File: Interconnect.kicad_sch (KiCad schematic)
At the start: 2 parts, among them J8 Interconnect-CPU, J9 Interconnect-PCH

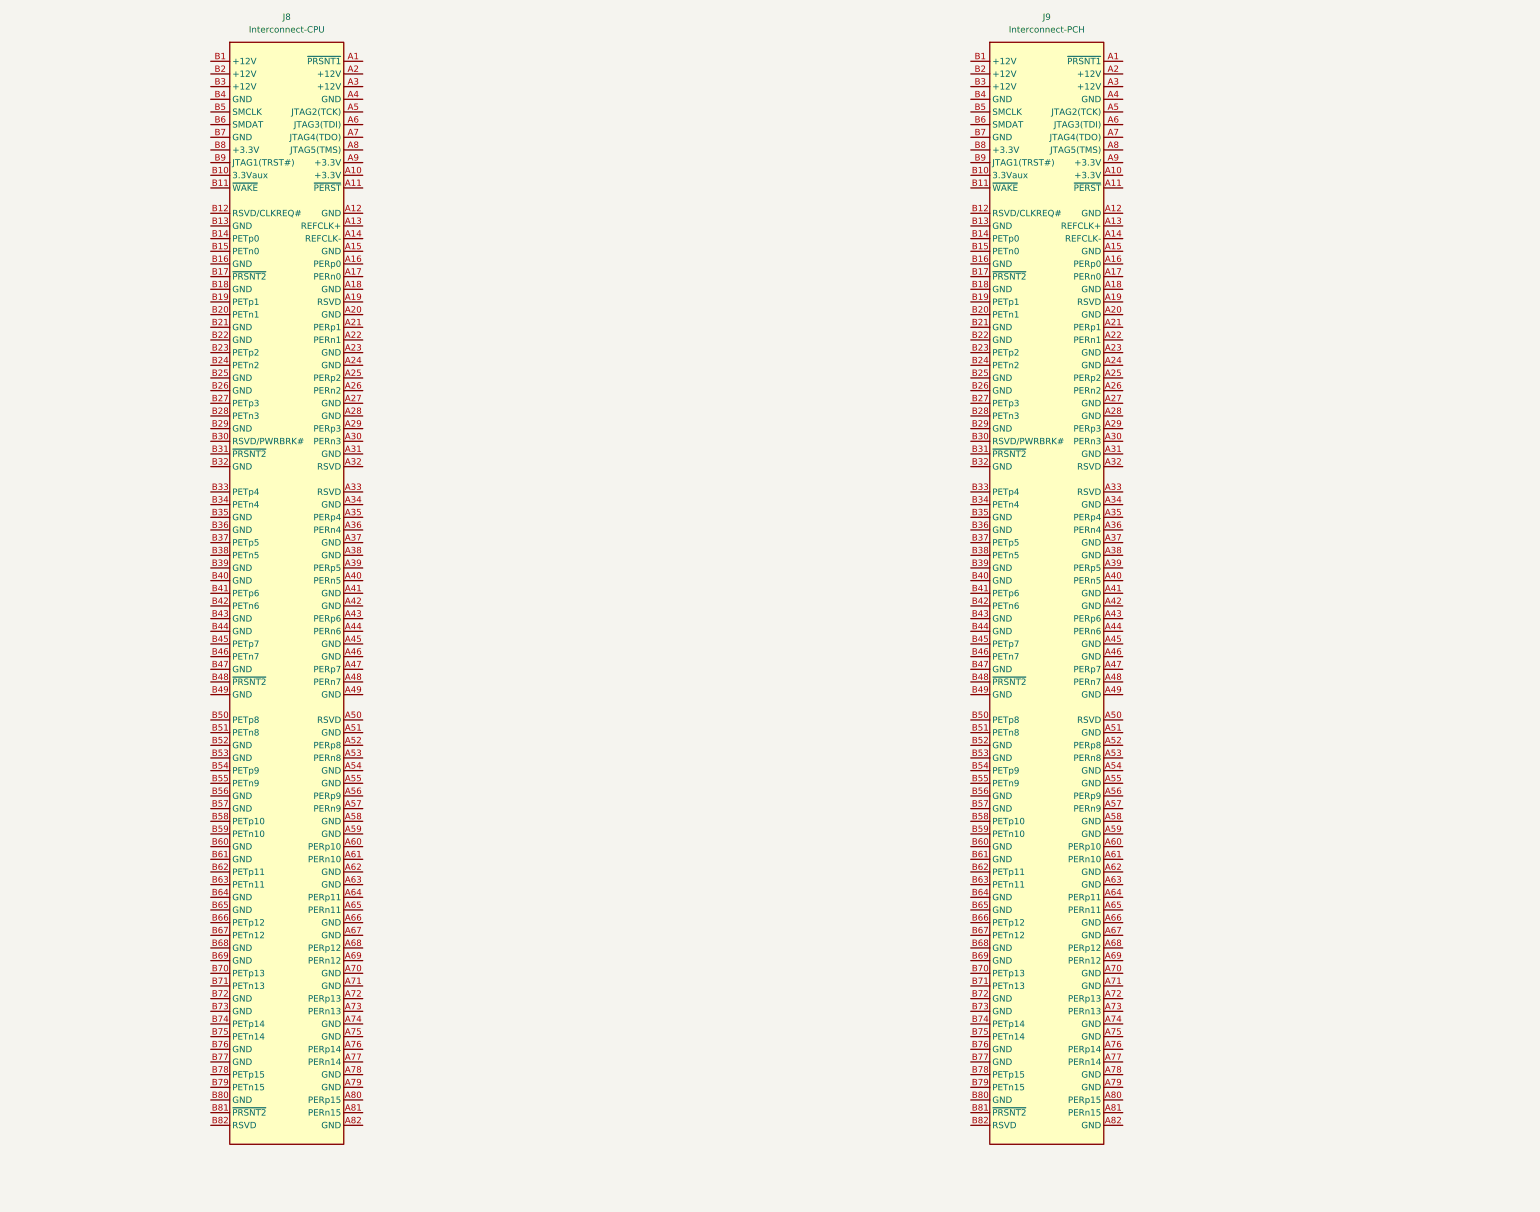
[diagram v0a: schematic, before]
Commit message: Added interconnect between CPU and PCH boards and added ATX board outline
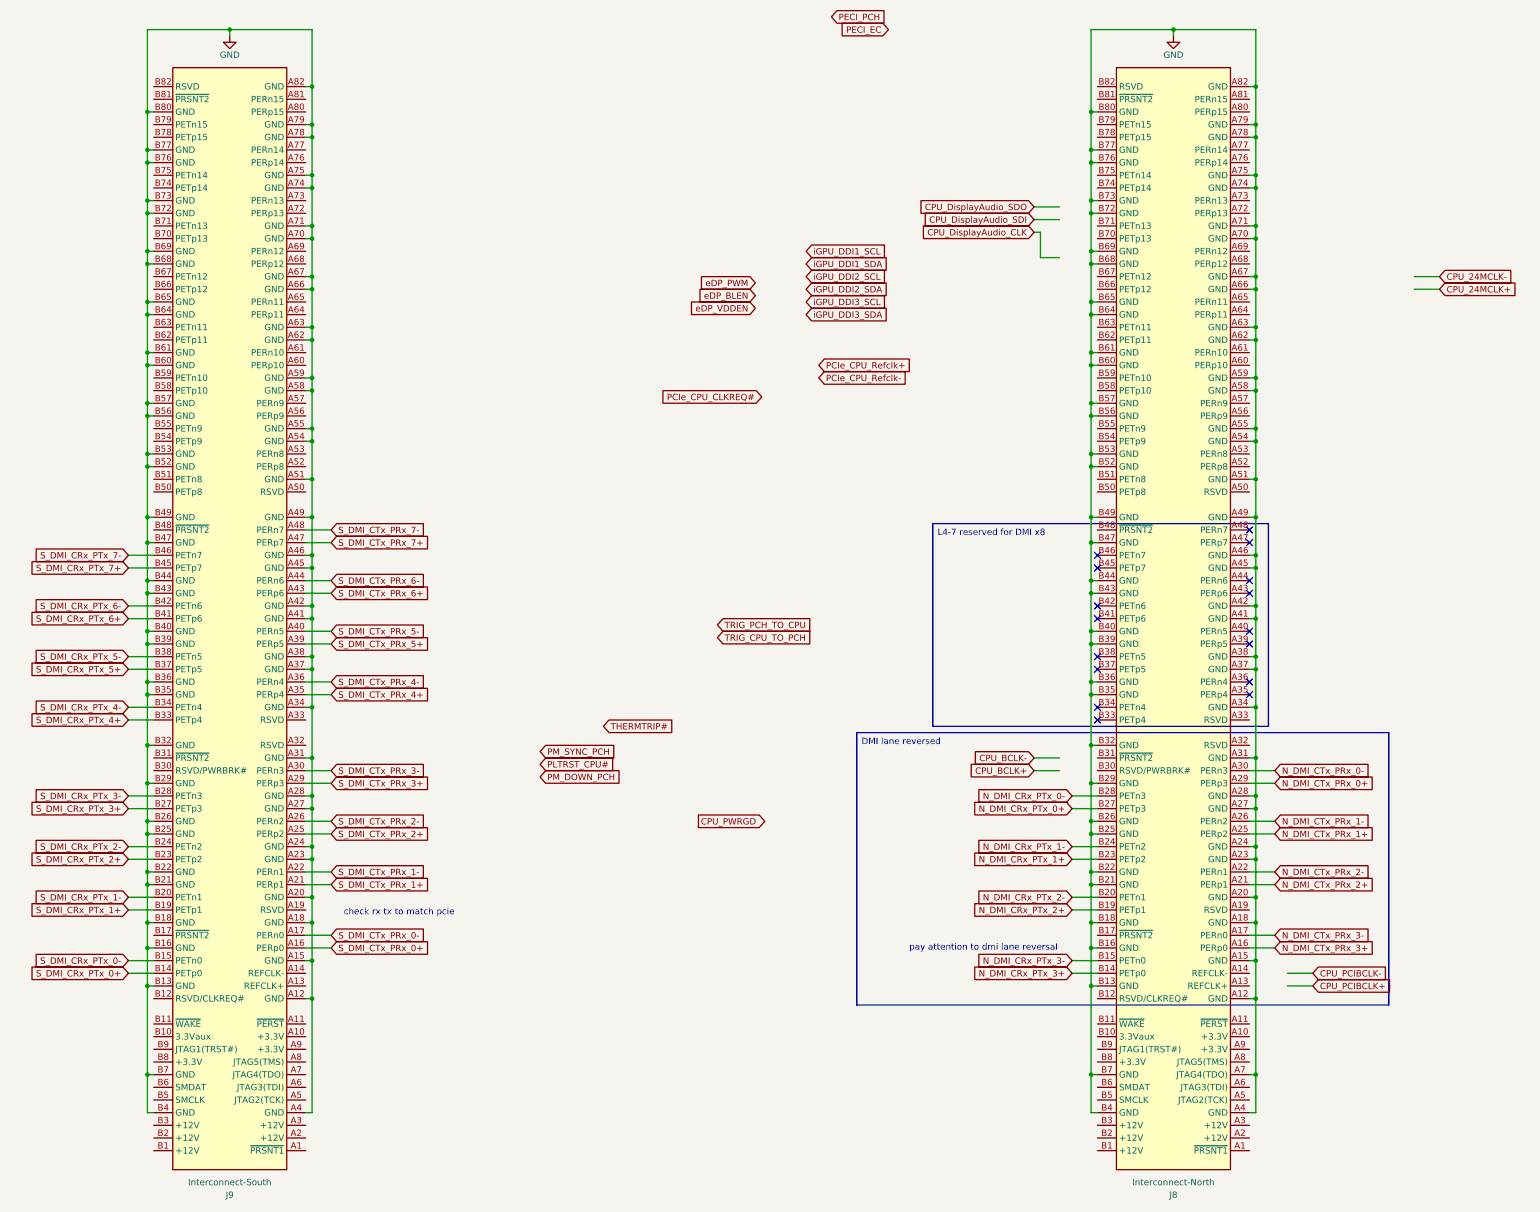
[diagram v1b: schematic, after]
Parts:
- J8: value Interconnect-CPU -> Interconnect-North; footprint Connector_PCBEdge:BUS_PCIexpress_x16 -> A-my-stuff:PCIe_x16_straddlemount
- J9: value Interconnect-PCH -> Interconnect-South
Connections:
- net GND: now reaches J9.A12 (GND)
- net GND: now also J8.A12 (GND), J8.A15 (GND), J8.A18 (GND), J8.A20 (GND), J8.A23 (GND), J8.A24 (GND), J8.A27 (GND), J8.A28 (GND), J8.A31 (GND), J8.A34 (GND), J8.A37 (GND), J8.A38 (GND), J8.A4 (GND), J8.A41 (GND), J8.A42 (GND), J8.A45 (GND), J8.A46 (GND), J8.A49 (GND), J8.A51 (GND), J8.A54 (GND), J8.A55 (GND), J8.A58 (GND), J8.A59 (GND), J8.A62 (GND), J8.A63 (GND), J8.A66 (GND), J8.A67 (GND), J8.A7 (JTAG4(TDO)), J8.A70 (GND), J8.A71 (GND), J8.A74 (GND), J8.A75 (GND), J8.A78 (GND), J8.A79 (GND), J8.A82 (GND), J8.B13 (GND), J8.B16 (GND), J8.B18 (GND), J8.B21 (GND), J8.B22 (GND), J8.B25 (GND), J8.B26 (GND), J8.B29 (GND), J8.B32 (GND), J8.B35 (GND), J8.B36 (GND), J8.B39 (GND), J8.B4 (GND), J8.B40 (GND), J8.B43 (GND), J8.B44 (GND), J8.B47 (GND), J8.B49 (GND), J8.B52 (GND), J8.B53 (GND), J8.B56 (GND), J8.B57 (GND), J8.B60 (GND), J8.B61 (GND), J8.B64 (GND), J8.B65 (GND), J8.B68 (GND), J8.B69 (GND), J8.B7 (GND), J8.B72 (GND), J8.B73 (GND), J8.B76 (GND), J8.B77 (GND), J8.B80 (GND), J9.A15 (GND), J9.A18 (GND), J9.A20 (GND), J9.A23 (GND), J9.A24 (GND), J9.A27 (GND), J9.A28 (GND), J9.A31 (GND), J9.A34 (GND), J9.A37 (GND), J9.A38 (GND), J9.A4 (GND), J9.A41 (GND), J9.A42 (GND), J9.A45 (GND), J9.A46 (GND), J9.A49 (GND), J9.A51 (GND), J9.A54 (GND), J9.A55 (GND), J9.A58 (GND), J9.A59 (GND), J9.A62 (GND), J9.A63 (GND), J9.A66 (GND), J9.A67 (GND), J9.A70 (GND), J9.A71 (GND), J9.A74 (GND), J9.A75 (GND), J9.A78 (GND), J9.A79 (GND), J9.A82 (GND), J9.B13 (GND), J9.B16 (GND), J9.B18 (GND), J9.B21 (GND), J9.B22 (GND), J9.B25 (GND), J9.B26 (GND), J9.B29 (GND), J9.B32 (GND), J9.B35 (GND), J9.B36 (GND), J9.B39 (GND), J9.B4 (GND), J9.B40 (GND), J9.B43 (GND), J9.B44 (GND), J9.B47 (GND), J9.B49 (GND), J9.B52 (GND), J9.B53 (GND), J9.B56 (GND), J9.B57 (GND), J9.B60 (GND), J9.B61 (GND), J9.B64 (GND), J9.B65 (GND), J9.B68 (GND), J9.B69 (GND), J9.B7 (GND), J9.B72 (GND), J9.B73 (GND), J9.B76 (GND), J9.B77 (GND), J9.B80 (GND)
- net S_DMI_CTx_PRx_0+: now reaches J9.A16 (PERp0)
- net S_DMI_CTx_PRx_0-: now reaches J9.A17 (PERn0)
- net S_DMI_CTx_PRx_1+: now reaches J9.A21 (PERp1)
- net S_DMI_CTx_PRx_1-: now reaches J9.A22 (PERn1)
- net S_DMI_CTx_PRx_2+: now reaches J9.A25 (PERp2)
- net S_DMI_CTx_PRx_2-: now reaches J9.A26 (PERn2)
- net S_DMI_CTx_PRx_3+: now reaches J9.A29 (PERp3)
- net S_DMI_CTx_PRx_3-: now reaches J9.A30 (PERn3)
- net S_DMI_CTx_PRx_4+: now reaches J9.A35 (PERp4)
- net S_DMI_CTx_PRx_4-: now reaches J9.A36 (PERn4)
- net S_DMI_CTx_PRx_5+: now reaches J9.A39 (PERp5)
- net S_DMI_CTx_PRx_5-: now reaches J9.A40 (PERn5)
- net S_DMI_CTx_PRx_6+: now reaches J9.A43 (PERp6)
- net S_DMI_CTx_PRx_6-: now reaches J9.A44 (PERn6)
- net S_DMI_CTx_PRx_7+: now reaches J9.A47 (PERp7)
- net S_DMI_CTx_PRx_7-: now reaches J9.A48 (PERn7)
- net S_DMI_CRx_PTx_0+: now reaches J9.B14 (PETp0)
- net S_DMI_CRx_PTx_0-: now reaches J9.B15 (PETn0)
- net S_DMI_CRx_PTx_1+: now reaches J9.B19 (PETp1)
- net S_DMI_CRx_PTx_1-: now reaches J9.B20 (PETn1)
- net S_DMI_CRx_PTx_2+: now reaches J9.B23 (PETp2)
- net S_DMI_CRx_PTx_2-: now reaches J9.B24 (PETn2)
- net S_DMI_CRx_PTx_3+: now reaches J9.B27 (PETp3)
- net S_DMI_CRx_PTx_3-: now reaches J9.B28 (PETn3)
- net S_DMI_CRx_PTx_4+: now reaches J9.B33 (PETp4)
- net S_DMI_CRx_PTx_4-: now reaches J9.B34 (PETn4)
- net S_DMI_CRx_PTx_5+: now reaches J9.B37 (PETp5)
- net S_DMI_CRx_PTx_5-: now reaches J9.B38 (PETn5)
- net S_DMI_CRx_PTx_6+: now reaches J9.B41 (PETp6)
- net S_DMI_CRx_PTx_6-: now reaches J9.B42 (PETn6)
- net S_DMI_CRx_PTx_7+: now reaches J9.B45 (PETp7)
- net S_DMI_CRx_PTx_7-: now reaches J9.B46 (PETn7)
- net N_DMI_CTx_PRx_3+: now reaches J8.A16 (PERp0)
- net N_DMI_CTx_PRx_3-: now reaches J8.A17 (PERn0)
- net N_DMI_CTx_PRx_2+: now reaches J8.A21 (PERp1)
- net N_DMI_CTx_PRx_2-: now reaches J8.A22 (PERn1)
- net N_DMI_CTx_PRx_1+: now reaches J8.A25 (PERp2)
- net N_DMI_CTx_PRx_1-: now reaches J8.A26 (PERn2)
- net N_DMI_CTx_PRx_0+: now reaches J8.A29 (PERp3)
- net N_DMI_CTx_PRx_0-: now reaches J8.A30 (PERn3)
- net N_DMI_CRx_PTx_3+: now reaches J8.B14 (PETp0)
- net N_DMI_CRx_PTx_3-: now reaches J8.B15 (PETn0)
- net N_DMI_CRx_PTx_2+: now reaches J8.B19 (PETp1)
- net N_DMI_CRx_PTx_2-: now reaches J8.B20 (PETn1)
- net N_DMI_CRx_PTx_1+: now reaches J8.B23 (PETp2)
- net N_DMI_CRx_PTx_1-: now reaches J8.B24 (PETn2)
- net N_DMI_CRx_PTx_0+: now reaches J8.B27 (PETp3)
- net N_DMI_CRx_PTx_0-: now reaches J8.B28 (PETn3)
- no-connect marks 0 -> 16
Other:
- note added: "check rx tx to match pcie"
- note added: "pay attention to dmi lane reversal"
- moved on the sheet: J8, J9
